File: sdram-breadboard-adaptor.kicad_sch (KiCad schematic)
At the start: 14 parts

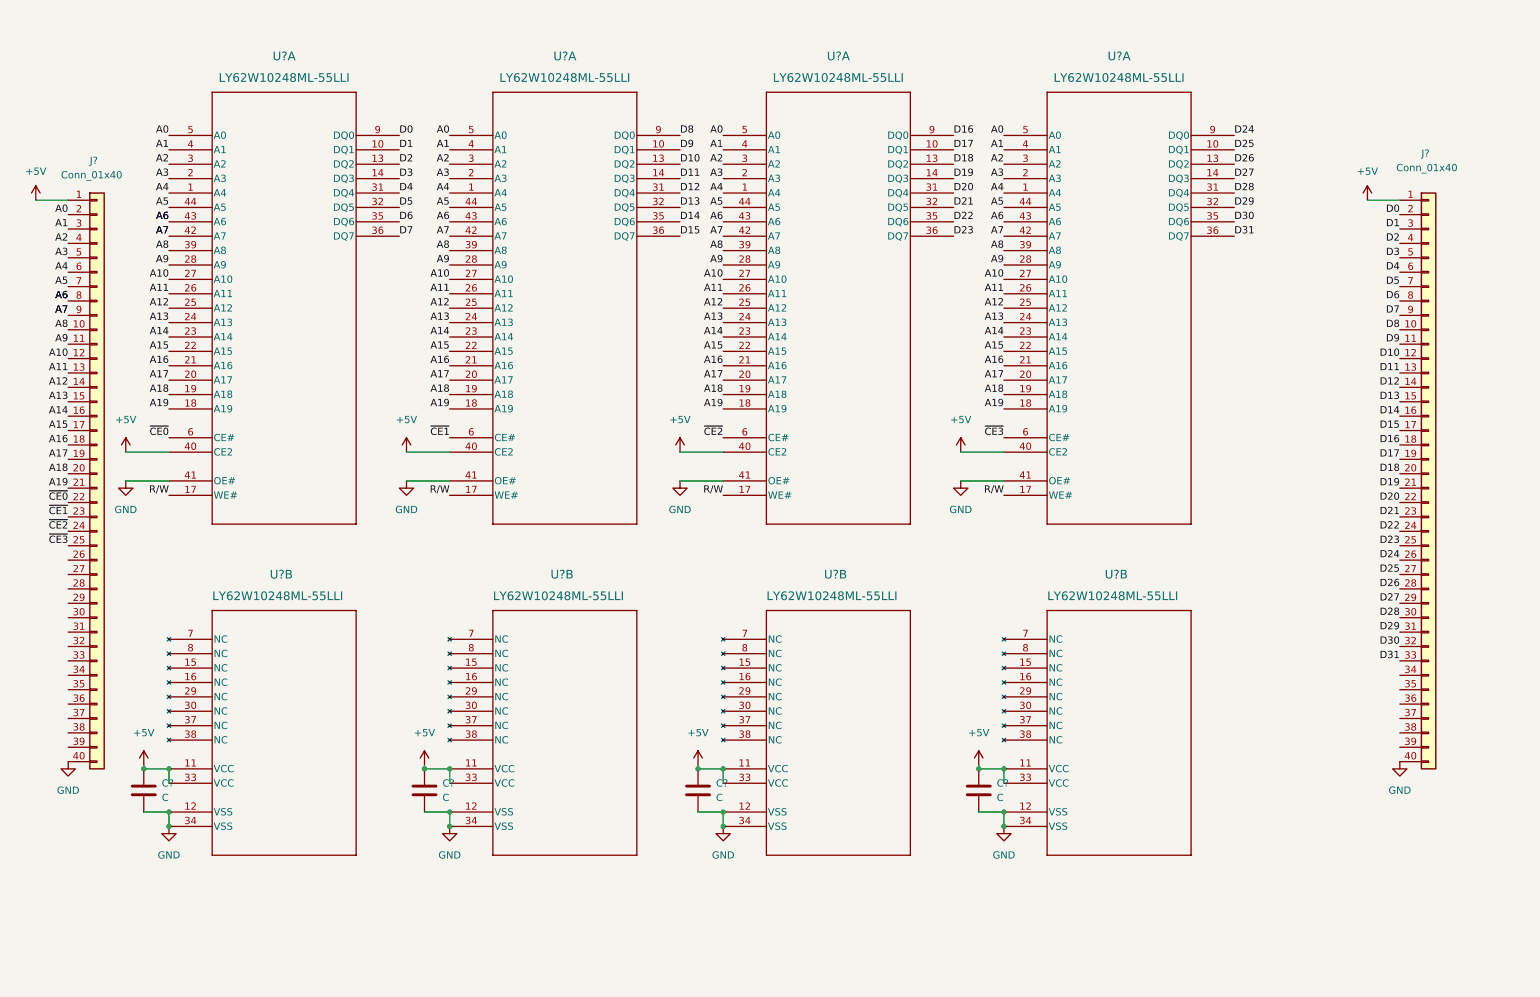
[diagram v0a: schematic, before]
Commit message: Add power flags
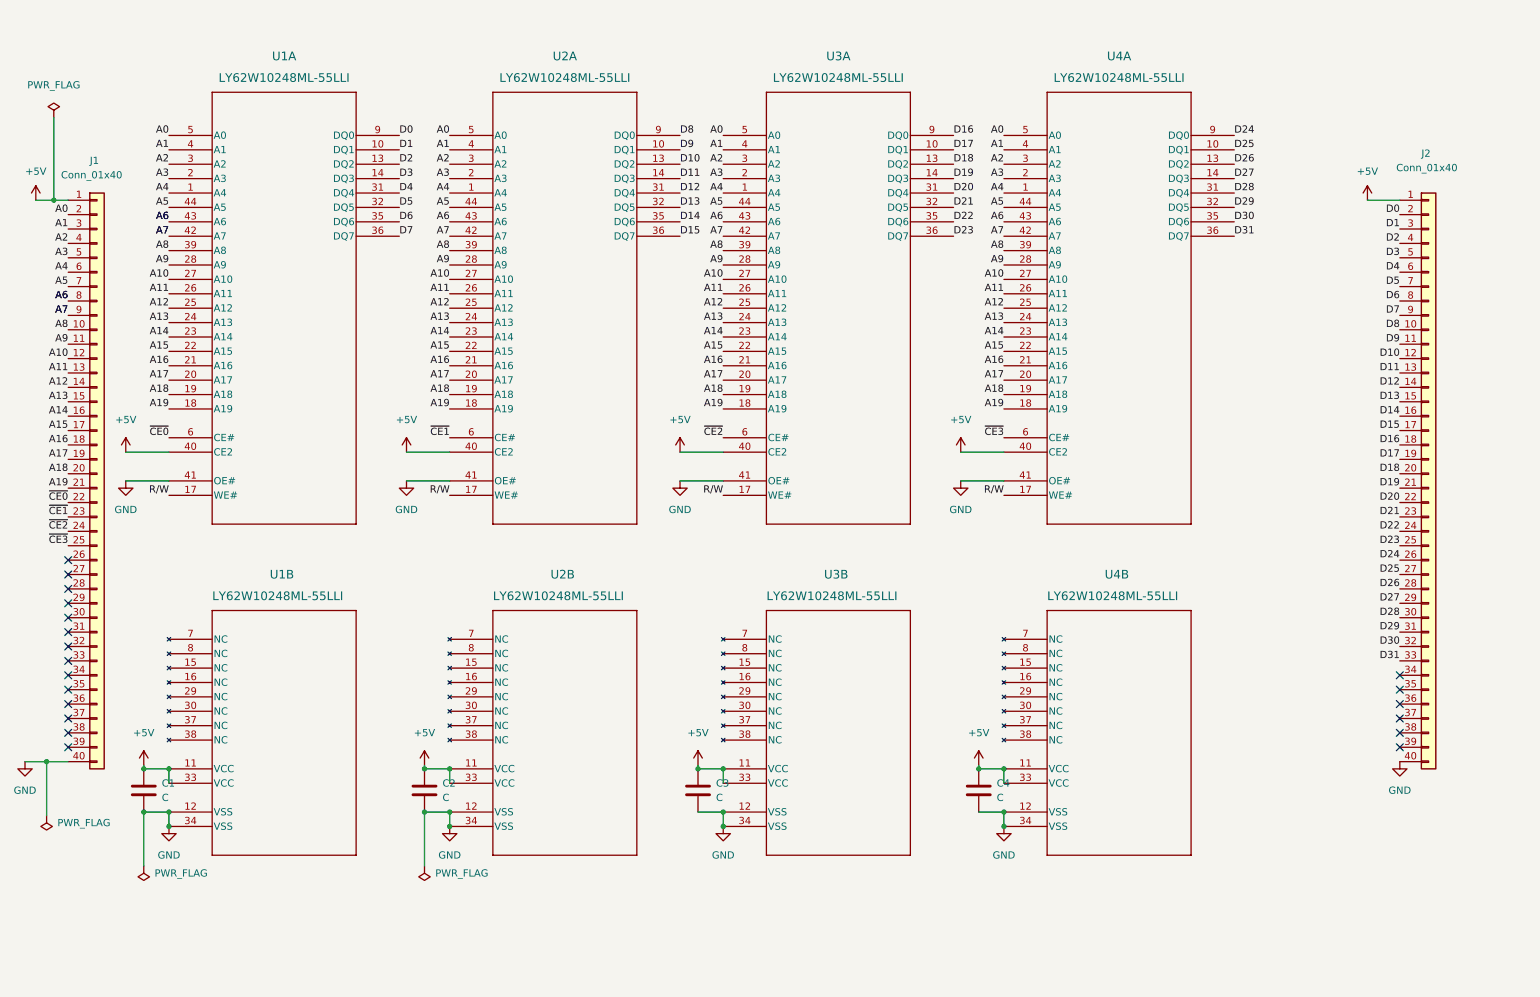
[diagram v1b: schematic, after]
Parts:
- gave numbers to parts that had none: 10
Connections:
- no-connect marks 0 -> 20

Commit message: Add pcb layout
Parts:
- removed C1, C2, C3, C4: C, symbol Device:C
- removed U1, U2, U3, U4: LY62W10248ML-55LLI, TSOP-II-44_400MIL_LTK, symbol 2023-06-02_15-35-47:LY62W10248ML-55LLI
- added U1, U2, U3, U4: LY62W10248ML-55LLI, TSOP-II-44_400MIL_LTK, symbol LYONTEK:LY62W10248ML-55LLI
- J1, J2: footprint (none) -> Connector_PinHeader_2.54mm:PinHeader_1x40_P2.54mm_Vertical
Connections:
- net A0 is gone; now on net A2: J1.2 (Pin_2)
- net A1 is gone; now on net A3: J1.3 (Pin_3)
- net A10: now also J1.10 (Pin_10), U1.39 (A8), U2.39 (A8), U3.39 (A8), U4.39 (A8); no longer J1.12 (Pin_12)
- net A11: now also J1.11 (Pin_11), U1.28 (A9), U2.28 (A9), U3.28 (A9), U4.28 (A9); no longer J1.13 (Pin_13)
- net A12: now also J1.12 (Pin_12), U1.27 (A10), U2.27 (A10), U3.27 (A10), U4.27 (A10); no longer J1.14 (Pin_14)
- net A13: now also J1.13 (Pin_13), U1.26 (A11), U2.26 (A11), U3.26 (A11), U4.26 (A11); no longer J1.15 (Pin_15)
- net A14: now also J1.14 (Pin_14), U1.25 (A12), U2.25 (A12), U3.25 (A12), U4.25 (A12); no longer J1.16 (Pin_16)
- net A15: now also J1.15 (Pin_15), U1.24 (A13), U2.24 (A13), U3.24 (A13), U4.24 (A13); no longer J1.17 (Pin_17)
- net A16: now also J1.16 (Pin_16), U1.23 (A14), U2.23 (A14), U3.23 (A14), U4.23 (A14); no longer J1.18 (Pin_18)
- net A17: now also J1.17 (Pin_17), U1.22 (A15), U2.22 (A15), U3.22 (A15), U4.22 (A15); no longer J1.19 (Pin_19)
- net A18: now also J1.18 (Pin_18), U1.21 (A16), U2.21 (A16), U3.21 (A16), U4.21 (A16); no longer J1.20 (Pin_20)
- net A19: now also J1.19 (Pin_19), U1.20 (A17), U2.20 (A17), U3.20 (A17), U4.20 (A17); no longer J1.21 (Pin_21)
- net A2: now also U1.5 (A0), U2.5 (A0), U3.5 (A0), U4.5 (A0); no longer J1.4 (Pin_4)
- net A3: now also U1.4 (A1), U2.4 (A1), U3.4 (A1), U4.4 (A1); no longer J1.5 (Pin_5)
- net A4: now also J1.4 (Pin_4), U1.3 (A2), U2.3 (A2), U3.3 (A2), U4.3 (A2); no longer J1.6 (Pin_6)
- net A5: now also J1.5 (Pin_5), U1.2 (A3), U2.2 (A3), U3.2 (A3), U4.2 (A3); no longer J1.7 (Pin_7)
- net A6: now also J1.6 (Pin_6), U1.1 (A4), U2.1 (A4), U3.1 (A4), U4.1 (A4); no longer J1.8 (Pin_8)
- net A7: now also J1.7 (Pin_7), U1.44 (A5), U2.44 (A5), U3.44 (A5), U4.44 (A5); no longer J1.9 (Pin_9)
- net A8: now also J1.8 (Pin_8), U1.43 (A6), U2.43 (A6), U3.43 (A6), U4.43 (A6); no longer J1.10 (Pin_10)
- net A9: now also J1.9 (Pin_9), U1.42 (A7), U2.42 (A7), U3.42 (A7), U4.42 (A7); no longer J1.11 (Pin_11)
- net D0: now also U1.9 (DQ0); no longer J2.2 (Pin_2)
- net D1: now also U1.10 (DQ1); no longer J2.3 (Pin_3)
- net D10: now also U2.13 (DQ2); no longer J2.12 (Pin_12)
- net D11: now also U2.14 (DQ3); no longer J2.13 (Pin_13)
- net D12: now also U2.31 (DQ4); no longer J2.14 (Pin_14)
- net D13: now also U2.32 (DQ5); no longer J2.15 (Pin_15)
- net D14: now also U2.35 (DQ6); no longer J2.16 (Pin_16)
- net D15: now also U2.36 (DQ7); no longer J2.17 (Pin_17)
- net D16: now also U3.9 (DQ0); no longer J2.18 (Pin_18)
- net D17: now also U3.10 (DQ1); no longer J2.19 (Pin_19)
- net D18: now also U3.13 (DQ2); no longer J2.20 (Pin_20)
- net D19: now also U3.14 (DQ3); no longer J2.21 (Pin_21)
- net D2: now also U1.13 (DQ2); no longer J2.4 (Pin_4)
- net D20: now also U3.31 (DQ4); no longer J2.22 (Pin_22)
- net D21: now also U3.32 (DQ5); no longer J2.23 (Pin_23)
- net D22: now also U3.35 (DQ6); no longer J2.24 (Pin_24)
- net D23: now also U3.36 (DQ7); no longer J2.25 (Pin_25)
- net D24: now also U4.9 (DQ0); no longer J2.26 (Pin_26)
- net D25: now also U4.10 (DQ1); no longer J2.27 (Pin_27)
- net D26: now also U4.13 (DQ2); no longer J2.28 (Pin_28)
- net D27: now also U4.14 (DQ3); no longer J2.29 (Pin_29)
- net D28: now also U4.31 (DQ4); no longer J2.30 (Pin_30)
- net D29: now also U4.32 (DQ5); no longer J2.31 (Pin_31)
- net D3: now also U1.14 (DQ3); no longer J2.5 (Pin_5)
- net D30: now also U4.35 (DQ6); no longer J2.32 (Pin_32)
- net D31: now also U4.36 (DQ7); no longer J2.33 (Pin_33)
- net D4: now also U1.31 (DQ4); no longer J2.6 (Pin_6)
- net D5: now also U1.32 (DQ5); no longer J2.7 (Pin_7)
- net D6: now also U1.35 (DQ6); no longer J2.8 (Pin_8)
- net D7: now also U1.36 (DQ7); no longer J2.9 (Pin_9)
- net D8: now also U2.9 (DQ0); no longer J2.10 (Pin_10)
- net D9: now also U2.10 (DQ1); no longer J2.11 (Pin_11)
- net +5V: no longer names the net of J1.1 (Pin_1)
- net +5V: no longer J2.1 (Pin_1)
- net GND: no longer names the net of J1.40 (Pin_40)
- net GND: no longer J2.40 (Pin_40)
- net ~{CE0}: no longer names the net of J1.22 (Pin_22)
- net ~{CE1}: no longer names the net of J1.23 (Pin_23)
- net ~{CE2}: no longer names the net of J1.24 (Pin_24)
- net ~{CE3}: no longer names the net of J1.25 (Pin_25)
- new net A20: J1.20 (Pin_20), U1.19 (A18), U2.19 (A18), U3.19 (A18), U4.19 (A18)
- new net A21: J1.21 (Pin_21), U1.18 (A19), U2.18 (A19), U3.18 (A19), U4.18 (A19)
- no-connect marks 20 -> 0

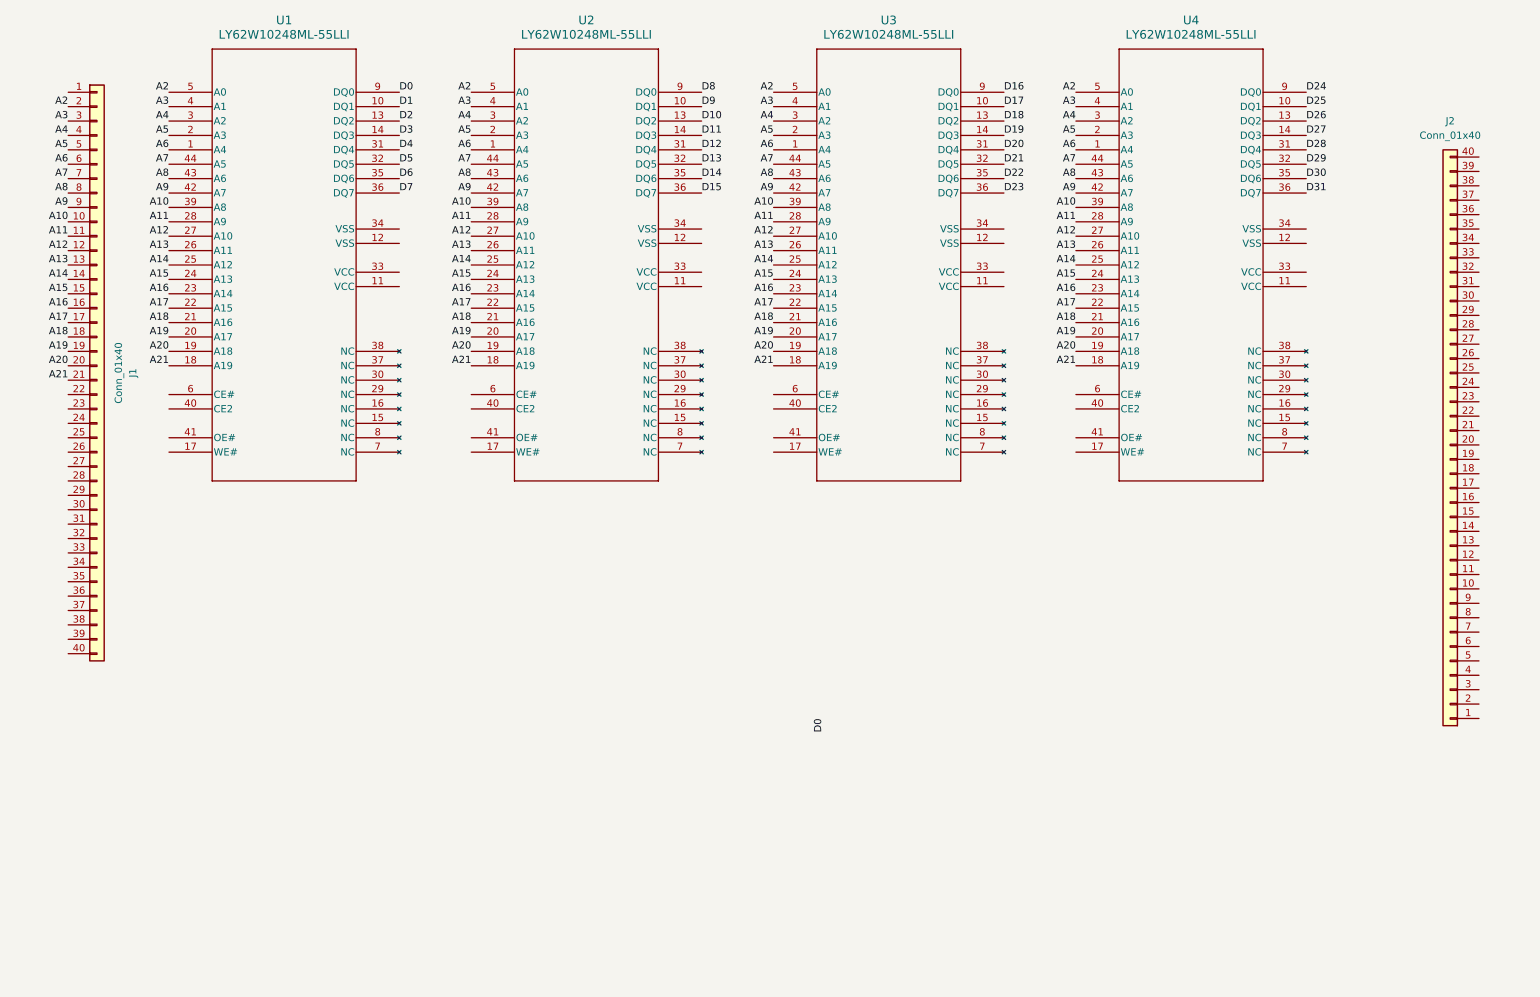
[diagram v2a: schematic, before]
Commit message: add 4 more chips
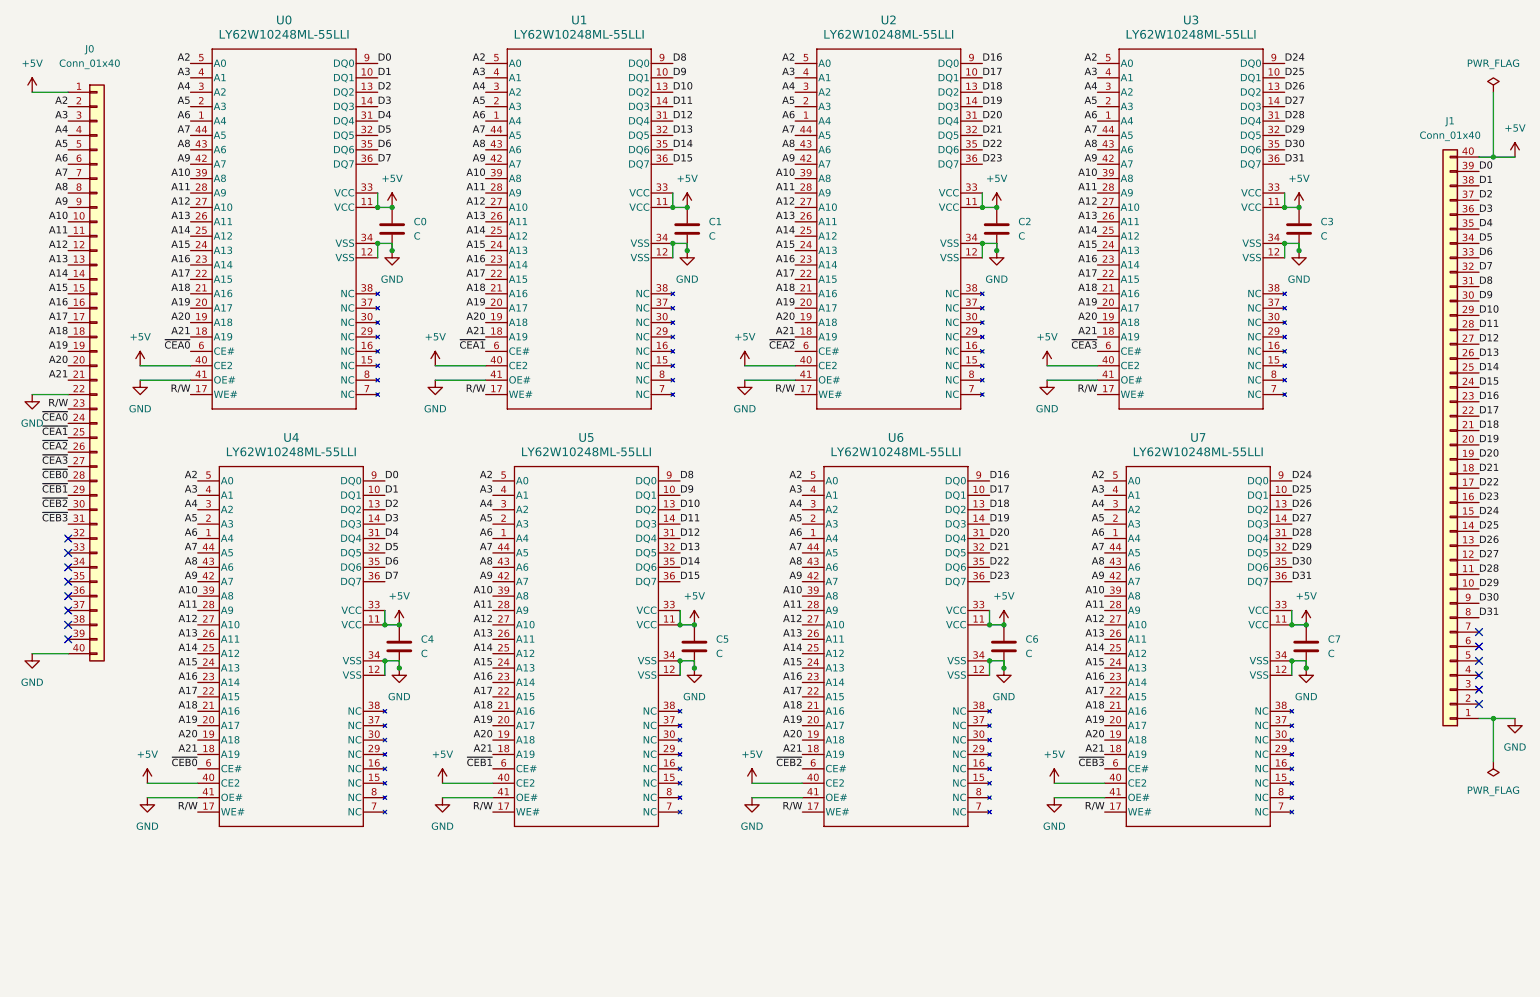
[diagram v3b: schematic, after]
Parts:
- added C0, C1, C2, C3, C4, C5, C6, C7: C, symbol Device:C
- added U1, U5, U6, U7: LY62W10248ML-55LLI, TSOP-II-44_400MIL_LTK, symbol LYONTEK:LY62W10248ML-55LLI
- renumbered J1 to J0, J2 to J1, U1 to U0
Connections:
- net A10: now also U1.39 (A8), U5.39 (A8), U6.39 (A8), U7.39 (A8)
- net A11: now also U1.28 (A9), U5.28 (A9), U6.28 (A9), U7.28 (A9)
- net A12: now also U1.27 (A10), U5.27 (A10), U6.27 (A10), U7.27 (A10)
- net A13: now also U1.26 (A11), U5.26 (A11), U6.26 (A11), U7.26 (A11)
- net A14: now also U1.25 (A12), U5.25 (A12), U6.25 (A12), U7.25 (A12)
- net A15: now also U1.24 (A13), U5.24 (A13), U6.24 (A13), U7.24 (A13)
- net A16: now also U1.23 (A14), U5.23 (A14), U6.23 (A14), U7.23 (A14)
- net A17: now also U1.22 (A15), U5.22 (A15), U6.22 (A15), U7.22 (A15)
- net A18: now also U1.21 (A16), U5.21 (A16), U6.21 (A16), U7.21 (A16)
- net A19: now also U1.20 (A17), U5.20 (A17), U6.20 (A17), U7.20 (A17)
- net A2: now also U1.5 (A0), U5.5 (A0), U6.5 (A0), U7.5 (A0)
- net A20: now also U1.19 (A18), U5.19 (A18), U6.19 (A18), U7.19 (A18)
- net A21: now also U1.18 (A19), U5.18 (A19), U6.18 (A19), U7.18 (A19)
- net A3: now also U1.4 (A1), U5.4 (A1), U6.4 (A1), U7.4 (A1)
- net A4: now also U1.3 (A2), U5.3 (A2), U6.3 (A2), U7.3 (A2)
- net A5: now also U1.2 (A3), U5.2 (A3), U6.2 (A3), U7.2 (A3)
- net A6: now also U1.1 (A4), U5.1 (A4), U6.1 (A4), U7.1 (A4)
- net A7: now also U1.44 (A5), U5.44 (A5), U6.44 (A5), U7.44 (A5)
- net A8: now also U1.43 (A6), U5.43 (A6), U6.43 (A6), U7.43 (A6)
- net A9: now also U1.42 (A7), U5.42 (A7), U6.42 (A7), U7.42 (A7)
- net D0: now also J1.39 (Pin_39), U4.9 (DQ0)
- net D1: now also J1.38 (Pin_38), U4.10 (DQ1)
- net D10: now also J1.29 (Pin_29), U1.13 (DQ2), U5.13 (DQ2); no longer U2.13 (DQ2)
- net D11: now also J1.28 (Pin_28), U1.14 (DQ3), U5.14 (DQ3); no longer U2.14 (DQ3)
- net D12: now also J1.27 (Pin_27), U1.31 (DQ4), U5.31 (DQ4); no longer U2.31 (DQ4)
- net D13: now also J1.26 (Pin_26), U1.32 (DQ5), U5.32 (DQ5); no longer U2.32 (DQ5)
- net D14: now also J1.25 (Pin_25), U1.35 (DQ6), U5.35 (DQ6); no longer U2.35 (DQ6)
- net D15: now also J1.24 (Pin_24), U1.36 (DQ7), U5.36 (DQ7); no longer U2.36 (DQ7)
- net D16: now also J1.23 (Pin_23), U2.9 (DQ0), U6.9 (DQ0); no longer U3.9 (DQ0)
- net D17: now also J1.22 (Pin_22), U2.10 (DQ1), U6.10 (DQ1); no longer U3.10 (DQ1)
- net D18: now also J1.21 (Pin_21), U2.13 (DQ2), U6.13 (DQ2); no longer U3.13 (DQ2)
- net D19: now also J1.20 (Pin_20), U2.14 (DQ3), U6.14 (DQ3); no longer U3.14 (DQ3)
- net D2: now also J1.37 (Pin_37), U4.13 (DQ2)
- net D20: now also J1.19 (Pin_19), U2.31 (DQ4), U6.31 (DQ4); no longer U3.31 (DQ4)
- net D21: now also J1.18 (Pin_18), U2.32 (DQ5), U6.32 (DQ5); no longer U3.32 (DQ5)
- net D22: now also J1.17 (Pin_17), U2.35 (DQ6), U6.35 (DQ6); no longer U3.35 (DQ6)
- net D23: now also J1.16 (Pin_16), U2.36 (DQ7), U6.36 (DQ7); no longer U3.36 (DQ7)
- net D24: now also J1.15 (Pin_15), U3.9 (DQ0), U7.9 (DQ0); no longer U4.9 (DQ0)
- net D25: now also J1.14 (Pin_14), U3.10 (DQ1), U7.10 (DQ1); no longer U4.10 (DQ1)
- net D26: now also J1.13 (Pin_13), U3.13 (DQ2), U7.13 (DQ2); no longer U4.13 (DQ2)
- net D27: now also J1.12 (Pin_12), U3.14 (DQ3), U7.14 (DQ3); no longer U4.14 (DQ3)
- net D28: now also J1.11 (Pin_11), U3.31 (DQ4), U7.31 (DQ4); no longer U4.31 (DQ4)
- net D29: now also J1.10 (Pin_10), U3.32 (DQ5), U7.32 (DQ5); no longer U4.32 (DQ5)
- net D3: now also J1.36 (Pin_36), U4.14 (DQ3)
- net D30: now also J1.9 (Pin_9), U3.35 (DQ6), U7.35 (DQ6); no longer U4.35 (DQ6)
- net D31: now also J1.8 (Pin_8), U3.36 (DQ7), U7.36 (DQ7); no longer U4.36 (DQ7)
- net D4: now also J1.35 (Pin_35), U4.31 (DQ4)
- net D5: now also J1.34 (Pin_34), U4.32 (DQ5)
- net D6: now also J1.33 (Pin_33), U4.35 (DQ6)
- net D7: now also J1.32 (Pin_32), U4.36 (DQ7)
- net D8: now also J1.31 (Pin_31), U1.9 (DQ0), U5.9 (DQ0); no longer U2.9 (DQ0)
- net D9: now also J1.30 (Pin_30), U1.10 (DQ1), U5.10 (DQ1); no longer U2.10 (DQ1)
- net +5V: now reaches U2.11 (VCC)
- net +5V: now also J0.1 (Pin_1), J1.40 (Pin_40), U0.11 (VCC), U0.33 (VCC), U0.40 (CE2), U2.33 (VCC), U2.40 (CE2), U3.11 (VCC), U3.33 (VCC), U3.40 (CE2), U4.11 (VCC), U4.33 (VCC), U4.40 (CE2), C0.1, C1.1, C2.1, C3.1, C4.1, C5.1, C6.1, C7.1, U1.11 (VCC), U1.33 (VCC), U1.40 (CE2), U5.11 (VCC), U5.33 (VCC), U5.40 (CE2), U6.11 (VCC), U6.33 (VCC), U6.40 (CE2), U7.11 (VCC), U7.33 (VCC), U7.40 (CE2)
- net GND: now reaches U2.12 (VSS)
- net GND: now also J0.22 (Pin_22), J0.40 (Pin_40), J1.1 (Pin_1), U0.12 (VSS), U0.34 (VSS), U0.41 (OE#), U2.34 (VSS), U2.41 (OE#), U3.12 (VSS), U3.34 (VSS), U3.41 (OE#), U4.12 (VSS), U4.34 (VSS), U4.41 (OE#), C0.2, C1.2, C2.2, C3.2, C4.2, C5.2, C6.2, C7.2, U1.12 (VSS), U1.34 (VSS), U1.41 (OE#), U5.12 (VSS), U5.34 (VSS), U5.41 (OE#), U6.12 (VSS), U6.34 (VSS), U6.41 (OE#), U7.12 (VSS), U7.34 (VSS), U7.41 (OE#)
- net R/W: now reaches U2.17 (WE#)
- net R/W: now also J0.23 (Pin_23), U0.17 (WE#), U3.17 (WE#), U4.17 (WE#), U1.17 (WE#), U5.17 (WE#), U6.17 (WE#), U7.17 (WE#)
- net ~{CEA2}: now reaches U2.6 (CE#)
- net ~{CEA2}: now also J0.26 (Pin_26)
- net ~{CEA0}: now reaches U0.6 (CE#)
- net ~{CEA0}: now also J0.24 (Pin_24)
- net ~{CEA1}: now reaches J0.25 (Pin_25)
- net ~{CEA1}: now also U1.6 (CE#)
- net ~{CEA3}: now reaches J0.27 (Pin_27)
- net ~{CEA3}: now also U3.6 (CE#)
- net ~{CEB0}: now reaches J0.28 (Pin_28)
- net ~{CEB0}: now also U4.6 (CE#)
- net ~{CEB1}: now reaches J0.29 (Pin_29)
- net ~{CEB1}: now also U5.6 (CE#)
- net ~{CEB2}: now reaches J0.30 (Pin_30)
- net ~{CEB2}: now also U6.6 (CE#)
- net ~{CEB3}: now reaches J0.31 (Pin_31)
- net ~{CEB3}: now also U7.6 (CE#)
- no-connect marks 0 -> 14
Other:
- moved on the sheet: U0
